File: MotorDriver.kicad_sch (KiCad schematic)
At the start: 14 parts, among them U1 DRV8323HRTAR

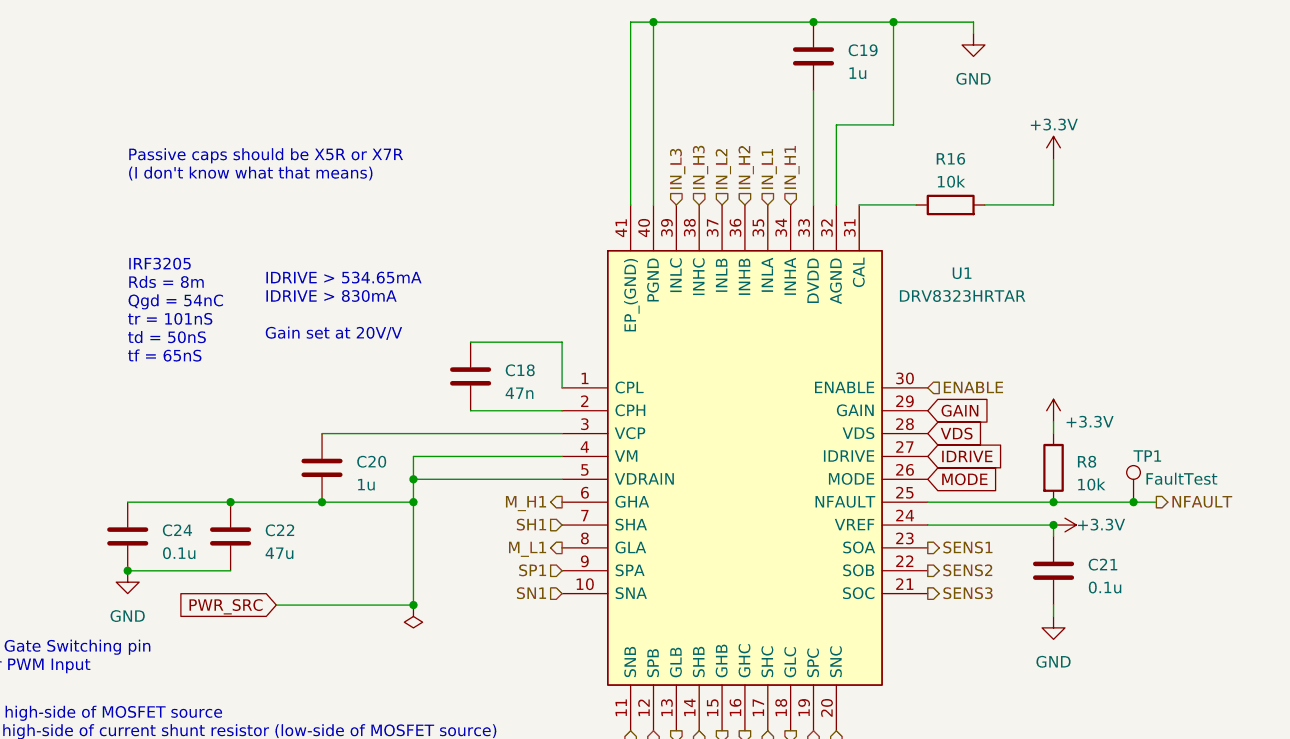
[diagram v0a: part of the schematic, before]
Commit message: Re-annotate all components
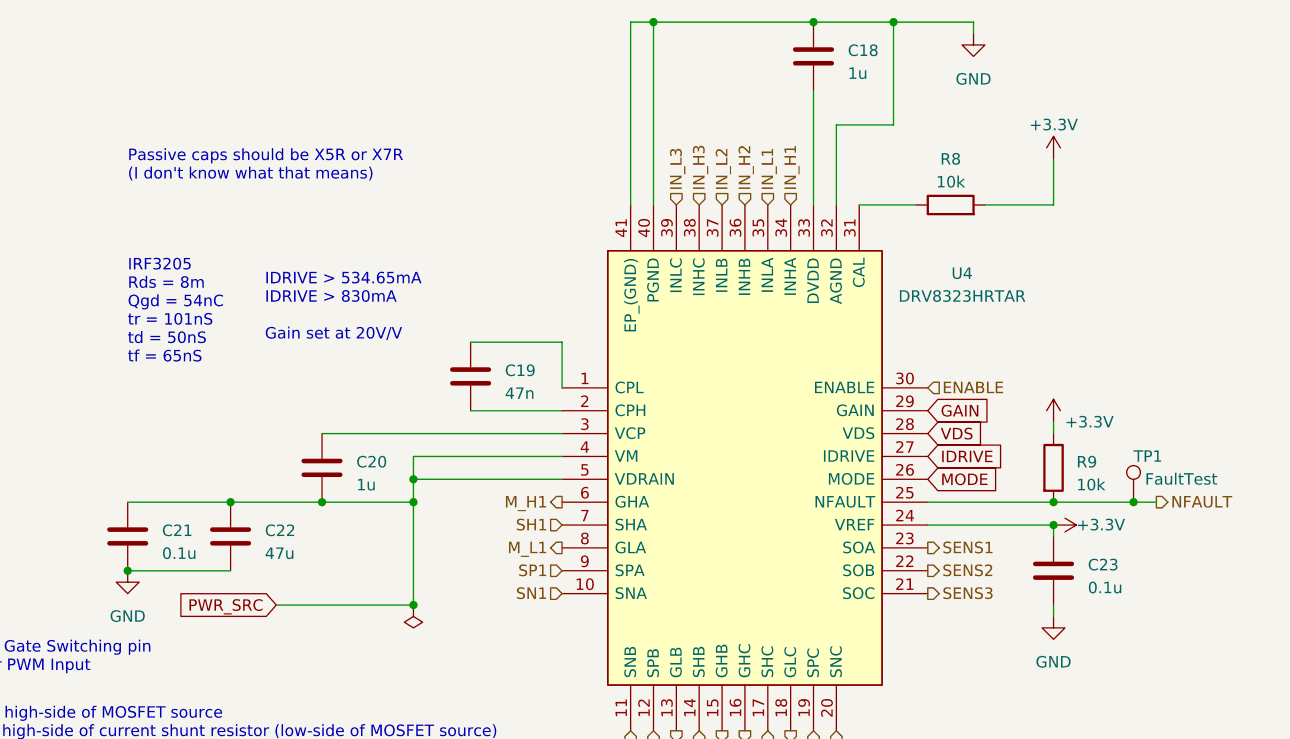
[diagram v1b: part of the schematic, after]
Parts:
- renumbered C19 to C18, C18 to C19, C24 to C21, C21 to C23, R16 to R8, R8 to R9, U1 to U4
